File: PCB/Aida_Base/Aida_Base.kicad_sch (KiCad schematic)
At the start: 106 parts, among them J1 AudioJack4, J10 Conn_01x04_Pin, J2 USB_C_Receptacle_L, J3 Conn_01x02_Pin, J4 Conn_01x03_Pin, J5 Conn_01x04_Pin, J6 Conn_01x04_Pin, J7 Conn_01x02_Pin, J8 Conn_02x02_Odd_Even, J9 Conn_01x03_Pin, Q1 BSS138, SW1 BOOT, SW2 RESET, U1 NCP1117-3.3_SOT223, U2 RP2040_L, U3 W25Q128JVS, Y1 12MHz

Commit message: 左手の回路が完成
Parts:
- removed H6: MountingHole_Pad, symbol Mechanical:MountingHole_Pad
- added H_btm_L1, H_btm_L2, H_btm_L3, H_btm_L4, H_btm_L5, H_btm_L6: MountingHole, Lib_Local:MountingHole_2.2mm_M2_No_Cu, symbol Mechanical:MountingHole
- added H_mid_L1, H_mid_L2: MountingHole, Lib_Local:MountingHole_1.8-2.2mm_M2_Pad_minimal, symbol Mechanical:MountingHole_Pad
- R12: value 100 -> 330
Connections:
- net GND_L: now also H_mid_L1.1, H_mid_L2.1
- no-connect marks 11 -> 12
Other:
- note added: "SCREWS to Bottom Plate"
- note added: "SCREWS to Mid"
- note added: "TRRSに 保護回路が あってもよい"
- note added: "Topへの Col4は 下のスイッチ と共通"
- moved on the sheet: C16, C17, C18, C19, D22, J1, J10, J3, J4, J5, J6, J7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

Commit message: PCBの部品配置をやり始めた。左右の部品を仕分けした。
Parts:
- removed J3: Conn_01x02_Pin, symbol Connector:Conn_01x02_Pin
- removed J4: Conn_01x03_Pin, symbol Connector:Conn_01x03_Pin
- added C13, C14, C15, C16, C17, C18, C19, C20, C25, C26, C36, C37, C38: 100n, Capacitor_SMD:C_0402_1005Metric, symbol Device:C_Small
- added C24, C29, C30: 2.2uF, Capacitor_SMD:C_0402_1005Metric, symbol Device:C_Small
- added C3, C4: 10u, Capacitor_SMD:C_0805_2012Metric, symbol Device:C_Small
- added C35: 4.7u, Capacitor_SMD:C_0402_1005Metric, symbol Device:C_Small
- added D10, D11, D12, D18, D19, D20, D21, D22, D29, D30, D31, D32, D33, D34, D39, D40, D41, D42, D46, D7, D8, D9: D, Lib_Local:D_SOD-123_Emphasized_Direction_Line, symbol Device:D
- added D44: PRTR5V0U2X, Package_TO_SOT_SMD:SOT-143, symbol Power_Protection:PRTR5V0U2X
- added F2: Fuse, Fuse:Fuse_0603_1608Metric, symbol Device:Polyfuse_Small
- added H10, H11, H12, H14, H16, H18, H20, H4, H5, H6, H9: MountingHole_Pad, Lib_Local:MountingHole_1.8-2.2mm_M2_Pad_minimal, symbol Mechanical:MountingHole_Pad
- added H_btm_R1, H_btm_R2, H_btm_R3, H_btm_R4, H_btm_R5, H_btm_R6: MountingHole, Lib_Local:MountingHole_2.2mm_M2_No_Cu, symbol Mechanical:MountingHole
- added H_mid_R1, H_mid_R2: MountingHole, Lib_Local:MountingHole_1.8-2.2mm_M2_Pad_minimal, symbol Mechanical:MountingHole_Pad
- added J10: Conn_01x03_Pin, Connector_PinHeader_2.54mm:PinHeader_1x03_P2.54mm_Vertical, symbol Connector:Conn_01x03_Pin
- added J12, J14, J16: Conn_01x04_Pin, Connector_PinHeader_2.54mm:PinHeader_1x04_P2.54mm_Vertical, symbol Connector:Conn_01x04_Pin
- added J18: Conn_02x02_Odd_Even, Connector_PinHeader_2.54mm:PinHeader_2x02_P2.54mm_Vertical, symbol Connector_Generic:Conn_02x02_Odd_Even
- added J2: AudioJack4, Connector_Audio:Jack_3.5mm_PJ320E_Horizontal, symbol Connector_Audio:AudioJack4
- added J4: USB_C_Receptacle_R, Connector_USB:USB_C_Receptacle_HRO_TYPE-C-31-M-12, symbol Connector:USB_C_Receptacle
- added J6: Conn_01x02_Pin, Connector_PinHeader_2.54mm:PinHeader_1x02_P2.54mm_Vertical, symbol Connector:Conn_01x02_Pin
- added J7, J8: Conn_01x05_Pin, Connector_PinHeader_2.54mm:PinHeader_1x05_P2.54mm_Vertical, symbol Connector:Conn_01x05_Pin
- added JP2: SolderJumper_2_Open, Jumper:SolderJumper-2_P1.3mm_Open_RoundedPad1.0x1.5mm, symbol Jumper:SolderJumper_2_Open
- added L4, L5, L6: SK6812MINI-E, Lib_Local:YS-SK6812MINI-E_middle_hole_with_small_pad, symbol kbd:SK6812MINI-E
- added LS2: Speaker, Buzzer_Beeper:Buzzer_Murata_PKMCS0909E, symbol Device:Speaker
- added Q2: BSS138, Package_TO_SOT_SMD:SOT-23, symbol Transistor_FET:BSS138
- added R10, R13, R14, R17, R2, R22: 1k, Resistor_SMD:R_0402_1005Metric, symbol Device:R_Small
- added R18, R4: 330, Resistor_SMD:R_0402_1005Metric, symbol Device:R_Small
- added R20: 10k, Resistor_SMD:R_0402_1005Metric, symbol Device:R_Small
- added R24, R26: 4.7k, Resistor_SMD:R_0402_1005Metric, symbol Device:R_Small
- added R6, R8: 5.1k, Resistor_SMD:R_0402_1005Metric, symbol Device:R_Small
- added SD2: Schottky diode, Diode_SMD:D_SOD-123, symbol Device:D_Shockley
- added STLED2: LED_GREEN, LED_SMD:LED_0201_0603Metric_Pad0.64x0.40mm_HandSolder, symbol Device:LED_Small
- added SW2: BOOT, Button_Switch_SMD:SW_SPST_PTS810, symbol Switch:SW_Push
- added SW4: RESET, Button_Switch_SMD:SW_SPST_PTS810, symbol Switch:SW_Push
- added SW_A2, SW_B2, SW_C2, SW_CMD_L2, SW_CTL2, SW_D2, SW_E2, SW_F2, SW_OPT_L2, SW_S2, SW_SPC2, SW_V2, SW_W2, SW_X2, SW_Z2: SW_Push, Lib_Local:Kailh_socket_ChocV2, symbol Switch:SW_Push
- added SW_RE_L2: RotaryEncoder_Switch, Lib_Local:ChocV2_AND_RotaryEncoder_Alps_EC11K-Switch_Vertical_H20mm_NPTH_MP_minimal, symbol Device:RotaryEncoder_Switch
- added U2: NCP1117-3.3_SOT223, Package_TO_SOT_SMD:SOT-223-3_TabPin2, symbol Regulator_Linear:NCP1117-3.3_SOT223
- added U4: RP2040_R, Package_DFN_QFN:QFN-56-1EP_7x7mm_P0.4mm_EP3.2x3.2mm, symbol MCU_RaspberryPi:RP2040
- added U6: W25Q128JVS, Package_SO:SOIC-8_5.3x5.3mm_P1.27mm, symbol Memory_Flash:W25Q128JVS
- added Y2: 12MHz, Crystal:Resonator_SMD_Murata_CSTxExxV-3Pin_3.0x1.1mm, symbol Device:Crystal_GND2
- D1, D2, D3, D4, D5, D6: footprint Diode_SMD:D_SOD-128 -> Lib_Local:D_SOD-123_Emphasized_Direction_Line
- D13: renamed from D7; footprint Diode_SMD:D_SOD-128 -> Lib_Local:D_SOD-123_Emphasized_Direction_Line
- D14: renamed from D8; footprint Diode_SMD:D_SOD-128 -> Lib_Local:D_SOD-123_Emphasized_Direction_Line
- D15: renamed from D9; footprint Diode_SMD:D_SOD-128 -> Lib_Local:D_SOD-123_Emphasized_Direction_Line
- D16: renamed from D10; footprint Diode_SMD:D_SOD-128 -> Lib_Local:D_SOD-123_Emphasized_Direction_Line
- D17: renamed from D11; footprint Diode_SMD:D_SOD-128 -> Lib_Local:D_SOD-123_Emphasized_Direction_Line
- D23: renamed from D12; footprint Diode_SMD:D_SOD-128 -> Lib_Local:D_SOD-123_Emphasized_Direction_Line
- D24: renamed from D13; footprint Diode_SMD:D_SOD-128 -> Lib_Local:D_SOD-123_Emphasized_Direction_Line
- D25: renamed from D14; footprint Diode_SMD:D_SOD-128 -> Lib_Local:D_SOD-123_Emphasized_Direction_Line
- D26: renamed from D15; footprint Diode_SMD:D_SOD-128 -> Lib_Local:D_SOD-123_Emphasized_Direction_Line
- D27: renamed from D16; footprint Diode_SMD:D_SOD-128 -> Lib_Local:D_SOD-123_Emphasized_Direction_Line
- D28: renamed from D17; footprint Diode_SMD:D_SOD-128 -> Lib_Local:D_SOD-123_Emphasized_Direction_Line
- D35: renamed from D18; footprint Diode_SMD:D_SOD-128 -> Lib_Local:D_SOD-123_Emphasized_Direction_Line
- D36: renamed from D19; footprint Diode_SMD:D_SOD-128 -> Lib_Local:D_SOD-123_Emphasized_Direction_Line
- D37: renamed from D20; footprint Diode_SMD:D_SOD-128 -> Lib_Local:D_SOD-123_Emphasized_Direction_Line
- D38: renamed from D21; footprint Diode_SMD:D_SOD-128 -> Lib_Local:D_SOD-123_Emphasized_Direction_Line
- D45: renamed from D22; footprint (none) -> Lib_Local:D_SOD-123_Emphasized_Direction_Line
- H1, H2, H3: footprint (none) -> Lib_Local:MountingHole_1.8-2.2mm_M2_Pad_minimal
- H13: renamed from H7; footprint (none) -> Lib_Local:MountingHole_1.8-2.2mm_M2_Pad_minimal
- H15: renamed from H8; footprint (none) -> Lib_Local:MountingHole_1.8-2.2mm_M2_Pad_minimal
- H17: renamed from H9; footprint (none) -> Lib_Local:MountingHole_1.8-2.2mm_M2_Pad_minimal
- H19: renamed from H10; footprint (none) -> Lib_Local:MountingHole_1.8-2.2mm_M2_Pad_minimal
- H7: renamed from H4; footprint (none) -> Lib_Local:MountingHole_1.8-2.2mm_M2_Pad_minimal
- H8: renamed from H5; footprint (none) -> Lib_Local:MountingHole_1.8-2.2mm_M2_Pad_minimal
- J1: footprint (none) -> Connector_Audio:Jack_3.5mm_PJ320E_Horizontal
- J11: renamed from J5; footprint (none) -> Connector_PinHeader_2.54mm:PinHeader_1x04_P2.54mm_Vertical
- J13: renamed from J10; footprint (none) -> Connector_PinHeader_2.54mm:PinHeader_1x04_P2.54mm_Vertical
- J15: renamed from J6; footprint (none) -> Connector_PinHeader_2.54mm:PinHeader_1x04_P2.54mm_Vertical
- J17: renamed from J8; footprint (none) -> Connector_PinHeader_2.54mm:PinHeader_2x02_P2.54mm_Vertical
- J5: renamed from J7; footprint (none) -> Connector_PinHeader_2.54mm:PinHeader_1x02_P2.54mm_Vertical
- J9: footprint (none) -> Connector_PinHeader_2.54mm:PinHeader_1x03_P2.54mm_Vertical
- R1: footprint (none) -> Resistor_SMD:R_0402_1005Metric
- R16: renamed from R13; footprint (none) -> Resistor_SMD:R_0402_1005Metric
- R19: renamed from R8; footprint (none) -> Resistor_SMD:R_0402_1005Metric
- R21: renamed from R9; footprint (none) -> Resistor_SMD:R_0402_1005Metric
- R23: renamed from R10; footprint (none) -> Resistor_SMD:R_0402_1005Metric
- R25: renamed from R11; footprint (none) -> Resistor_SMD:R_0402_1005Metric
- R3: renamed from R12; footprint (none) -> Resistor_SMD:R_0402_1005Metric
- renumbered C8 to C10, C9 to C11, C10 to C12, C11 to C21, C14 to C22, C15 to C23, C12 to C27, C13 to C28, C16 to C31, C17 to C32, C18 to C33, C19 to C34, C3 to C5, C4 to C6, C5 to C7, C6 to C8, C7 to C9, D23 to D43, J2 to J3, R4 to R11, R5 to R12, R3 to R15, R6 to R5, R2 to R9, SW2 to SW3, U2 to U3, U3 to U5
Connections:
- net COL_L_4: now also H9.1
- net GPIO00 renamed GPIO00_L
- net GPIO00_L: now also J7.1 (Pin_1)
- net GPIO01 renamed GPIO01_L
- net GPIO01_L: now also J7.2 (Pin_2)
- net GPIO11 renamed GPIO11_L
- net GPIO11_L: now also J7.3 (Pin_3)
- net GPIO12 renamed GPIO12_L
- net GPIO12_L: now also J7.4 (Pin_4)
- net GPIO13 renamed GPIO13_L
- net GPIO13_L: now also J7.5 (Pin_5)
- net GPIO22 renamed GPIO22_L
- net GPIO23 renamed GPIO23_L
- net GPIO24 renamed GPIO24_L
- net GPIO25 renamed GPIO25_L
- net GPIO26 renamed GPIO26_L
- net GPIO27 renamed GPIO27_L
- net GPIO28 renamed GPIO28_L
- net GPIO29 renamed GPIO29_L
- new net: D8.2 (A), SW_W2.2
- new net: L4.4 (DIN), R18.2
- new net: LS2.1, R10.1
- new net: D20.2 (A), SW_D2.2
- new net: D40.2 (A), SW_CMD_L2.2
- new net: D19.2 (A), SW_S2.2
- new net: D7.2 (A), H4.1
- new net: J4.A5 (CC1), R6.1
- new net: D42.2 (A), SW_CTL2.2
- new net: R2.2, STLED2.2 (A)
- new net: D10.2 (A), H5.1
- new net: D32.2 (A), SW_V2.2
- new net: U4.20 (XIN), Y2.1
- new net: R17.1, Y2.3
- new net: JP2.2 (B), R2.1
- new net: D11.2 (A), H6.1
- new net: D29.2 (A), SW_Z2.2
- new net: D30.2 (A), SW_X2.2
- new net: J2.R1, R4.1
- new net: D18.2 (A), SW_A2.2
- new net: D39.2 (A), SW_OPT_L2.2
- new net: D21.2 (A), SW_F2.2
- new net: D34.2 (A), H18.1
- new net: D12.2 (A), SW_RE_L2.S2
- new net: L4.2 (DOUT), L5.4 (DIN)
- new net: L5.2 (DOUT), L6.4 (DIN)
- new net: J4.B5 (CC2), R8.1
- new net: F2.2, SD2.2 (A)
- new net: D9.2 (A), SW_E2.2
- new net: D31.2 (A), SW_C2.2
- new net: D33.2 (A), SW_B2.2
- new net: D22.2 (A), H14.1
- new net: R17.2, U4.21 (XOUT)
- new net: D41.2 (A), SW_SPC2.2
- new net +1V1_R: C25.1, C26.1, C30.1, U4.23 (DVDD), U4.45 (VREG_VOUT), U4.50 (DVDD)
- new net +3V3_R: C13.1, C14.1, C15.1, C16.1, C17.1, C18.1, C19.1, C20.1, C24.1, C29.1, C4.1, J14.1 (Pin_1), J6.2 (Pin_2), JP2.1 (A), Q2.1 (G), R13.2, R20.1, R24.1, R26.2, U2.2 (VO), U4.1 (IOVDD), U4.10 (IOVDD), U4.22 (IOVDD), U4.33 (IOVDD), U4.42 (IOVDD), U4.43 (ADC_AVDD), U4.44 (VREG_VIN), U4.48 (USB_VDD), U4.49 (IOVDD), U6.8 (VCC)
- new net +5V_R: C3.1, C35.2, C36.2, C37.2, C38.2, J2.T, J6.1 (Pin_1), L4.1 (VDD), L5.1 (VDD), L6.1 (VDD), R14.2, SD2.1 (K), U2.3 (VI)
- new net BUZZ_R: D46.1 (K), R10.2, U4.30 (GPIO19)
- new net COL_R_0: H10.1, SW_A2.1, SW_Z2.1, U4.8 (GPIO6)
- new net COL_R_1: SW_S2.1, SW_W2.1, SW_X2.1, U4.9 (GPIO7)
- new net COL_R_2: SW_C2.1, SW_D2.1, SW_E2.1, SW_OPT_L2.1, U4.11 (GPIO8)
- new net COL_R_3: H11.1, SW_CMD_L2.1, SW_F2.1, SW_V2.1, U4.12 (GPIO9)
- new net COL_R_4: H12.1, H16.1, SW_B2.1, SW_SPC2.1, U4.13 (GPIO10)
- new net COL_R_5: H20.1, SW_CTL2.1, SW_RE_L2.S1, U4.18 (GPIO15)
- new net D+_R: D44.2 (I/O1), J4.A6 (D+), J4.B6 (D+), U4.47 (USB_DP)
- new net D-_R: D44.3 (I/O2), J4.A7 (D-), J4.B7 (D-), U4.46 (USB_DM)
- new net DATA_R: R4.2, U4.17 (GPIO14)
- new net ENC_R_A: SW_RE_L2.A, U4.28 (GPIO17)
- new net ENC_R_B: SW_RE_L2.B, U4.29 (GPIO18)
- new net GND_R: C13.2, C14.2, C15.2, C16.2, C17.2, C18.2, C19.2, C20.2, C24.2, C25.2, C26.2, C29.2, C3.2, C30.2, C35.1, C36.1, C37.1, C38.1, C4.2, D44.1 (GND), D46.2 (A), H_mid_R1.1, H_mid_R2.1, J10.2 (Pin_2), J14.4 (Pin_4), J18.2 (Pin_2), J18.4 (Pin_4), J2.R2, J2.S, J4.A1 (GND), J4.A12 (GND), J4.B1 (GND), J4.B12 (GND), J4.S1 (SHIELD), L4.3 (GND), L5.3 (GND), L6.3 (GND), LS2.2, R6.2, R8.2, STLED2.1 (K), SW2.2, SW4.2, SW_RE_L2.C, U2.1 (GND), U4.19 (TESTEN), U4.57 (GND), U6.4 (GND), Y2.2
- new net GPIO00_R: J8.1 (Pin_1), U4.2 (GPIO0)
- new net GPIO01_R: J8.2 (Pin_2), U4.3 (GPIO1)
- new net GPIO11_R: J8.3 (Pin_3), U4.14 (GPIO11)
- new net GPIO12_R: J8.4 (Pin_4), U4.15 (GPIO12)
- new net GPIO13_R: J8.5 (Pin_5), U4.16 (GPIO13)
- new net GPIO22_R: J12.1 (Pin_1), U4.34 (GPIO22)
- new net GPIO23_R: J12.2 (Pin_2), U4.35 (GPIO23)
- new net GPIO24_R: J12.3 (Pin_3), U4.36 (GPIO24)
- new net GPIO25_R: J12.4 (Pin_4), U4.37 (GPIO25)
- new net GPIO26_R: J16.1 (Pin_1), U4.38 (GPIO26/ADC0)
- new net GPIO27_R: J16.2 (Pin_2), U4.39 (GPIO27/ADC1)
- new net GPIO28_R: J16.3 (Pin_3), U4.40 (GPIO28/ADC2)
- new net GPIO29_R: J16.4 (Pin_4), U4.41 (GPIO29/ADC3)
- new net LED_3V3_R: Q2.2 (S), R13.1, U4.27 (GPIO16)
- new net LED_5V_R: Q2.3 (D), R14.1, R18.1
- new net QSPI_SCLK_R: U4.52 (QSPI_SCLK), U6.6 (CLK)
- new net QSPI_SD0_R: U4.53 (QSPI_SD0), U6.5 (DI/IO_{0})
- new net QSPI_SD1_R: U4.55 (QSPI_SD1), U6.2 (DO/IO_{1})
- new net QSPI_SD2_R: U4.54 (QSPI_SD2), U6.3 (~{WP}/IO_{2})
- new net QSPI_SD3_R: U4.51 (QSPI_SD3), U6.7 (~{HOLD}/~{RESET}/IO_{3})
- new net QSPI_SS_R: R20.2, R22.1, U4.56 (~{QSPI_SS}), U6.1 (~{CS})
- new net RESET_R: J18.3 (Pin_3), SW4.1, U4.26 (RUN)
- new net ROW_R_0: D10.1 (K), D11.1 (K), D12.1 (K), D7.1 (K), D8.1 (K), D9.1 (K), U4.4 (GPIO2)
- new net ROW_R_1: D18.1 (K), D19.1 (K), D20.1 (K), D21.1 (K), D22.1 (K), U4.5 (GPIO3)
- new net ROW_R_2: D29.1 (K), D30.1 (K), D31.1 (K), D32.1 (K), D33.1 (K), D34.1 (K), U4.6 (GPIO4)
- new net ROW_R_3: D39.1 (K), D40.1 (K), D41.1 (K), D42.1 (K), U4.7 (GPIO5)
- new net SCL_R: J14.3 (Pin_3), R26.1, U4.32 (GPIO21)
- new net SDA_R: J14.2 (Pin_2), R24.2, U4.31 (GPIO20)
- new net SWCLK_R: J10.1 (Pin_1), U4.24 (SWCLK)
- new net SWDIO_R: J10.3 (Pin_3), U4.25 (SWDIO)
- new net USB_BOOT_R: J18.1 (Pin_1), R22.2, SW2.1
- new net VBUS_R: D44.4 (VCC), F2.1, J4.A4 (VBUS), J4.A9 (VBUS), J4.B4 (VBUS), J4.B9 (VBUS)
- no-connect marks 12 -> 22
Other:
- moved on the sheet: J11, J15

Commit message: 左手パーツ配置中。右手マトリクス修正
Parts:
- removed SW_A2, SW_B2, SW_C2, SW_CMD_L2, SW_CTL2, SW_D2, SW_E2, SW_F2, SW_OPT_L2, SW_S2, SW_SPC2, SW_V2, SW_W2, SW_X2, SW_Z2: SW_Push, Lib_Local:Kailh_socket_ChocV2, symbol Switch:SW_Push
- added SW_-1, SW_/1, SW_<1, SW_>1, SW_BS1, SW_CMD_R1, SW_ENT1, SW_I1, SW_J1, SW_K1, SW_L1, SW_M1, SW_N1, SW_O1, SW_OPT_R1: SW_Push, Lib_Local:Kailh_socket_ChocV2, symbol Switch:SW_Push
- D6, H10, SW_RE_L1: now not fitted
- H1: value MountingHole_Pad -> COL_L_0_from_Mid_Outside
- H12: now fitted
- H13: value MountingHole_Pad -> COL_L_4_from_Mid_Inside
- H15: value MountingHole_Pad -> COL_L_4_to_Mid_Inside
- H17: value MountingHole_Pad -> COL_L_5_from_Mid_Inside
- H19: value MountingHole_Pad -> COL_L_5_to_Mid_Inside
- H2: value MountingHole_Pad -> COL_L_3_from_Mid_Inside
- H3: value MountingHole_Pad -> COL_L_4_from_Top
- H7: value MountingHole_Pad -> COL_L_0_to_Mid_Outside
- H8: value MountingHole_Pad -> COL_L_3_to_Mid_Inside
- J11, J12, J15, J16: footprint Connector_PinHeader_2.54mm:PinHeader_1x04_P2.54mm_Vertical -> Connector_PinHeader_1.00mm:PinHeader_1x04_P1.00mm_Vertical
- J17, J18: footprint Connector_PinHeader_2.54mm:PinHeader_2x02_P2.54mm_Vertical -> Connector_PinHeader_2.00mm:PinHeader_2x02_P2.00mm_Vertical
- J5, J6: footprint Connector_PinHeader_2.54mm:PinHeader_1x02_P2.54mm_Vertical -> Connector_PinHeader_2.00mm:PinHeader_1x02_P2.00mm_Vertical
- J7, J8: footprint Connector_PinHeader_2.54mm:PinHeader_1x05_P2.54mm_Vertical -> Connector_PinHeader_1.00mm:PinHeader_1x05_P1.00mm_Vertical
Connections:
- net COL_R_0: now also H12.1, SW_-1.1, SW_/1.1; no longer H10.1
- net COL_R_1: now also SW_>1.1, SW_L1.1, SW_O1.1
- net COL_R_2: now also SW_<1.1, SW_I1.1, SW_K1.1, SW_OPT_R1.1
- net COL_R_3: now also SW_CMD_R1.1, SW_J1.1, SW_M1.1
- net COL_R_4: now also H10.1, SW_ENT1.1, SW_N1.1; no longer H12.1
- net COL_R_5: now also SW_BS1.1
- net at D8.2 (A): now also H4.1
- net at D20.2 (A): now also SW_K1.2
- net at D40.2 (A): now also SW_ENT1.2
- net at D19.2 (A): now also SW_J1.2
- net at D7.2 (A): now also SW_RE_L2.S2; no longer H4.1
- net at D42.2 (A): now also SW_OPT_R1.2
- net at D10.2 (A): now also SW_I1.2; no longer H5.1
- net at D32.2 (A): now also SW_<1.2
- net at D11.2 (A): now also SW_O1.2; no longer H6.1
- net at D29.2 (A): now also H18.1
- net at D30.2 (A): now also SW_N1.2
- net at D18.2 (A): now also H14.1
- net at D39.2 (A): now also SW_BS1.2
- net at D21.2 (A): now also SW_L1.2
- net at D34.2 (A): now also SW_/1.2; no longer H18.1
- net at D12.2 (A): now also H6.1; no longer SW_RE_L2.S2
- net at D9.2 (A): now also H5.1
- net at D31.2 (A): now also SW_M1.2
- net at D33.2 (A): now also SW_>1.2
- net at D22.2 (A): now also SW_-1.2; no longer H14.1
- net at D41.2 (A): now also SW_CMD_R1.2
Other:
- moved on the sheet: C1, C2, C3, C4

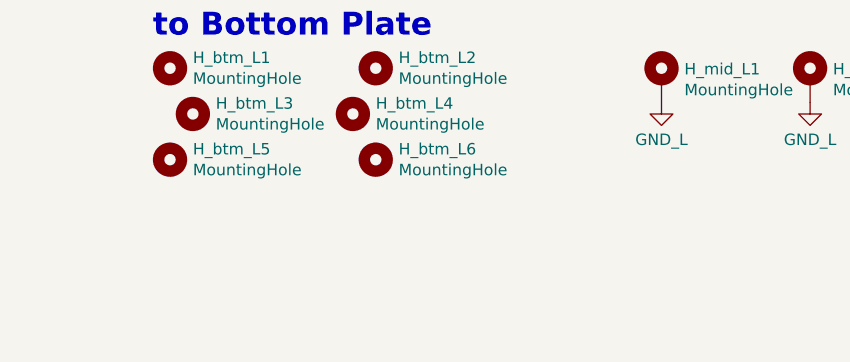
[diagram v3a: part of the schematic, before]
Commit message: 左手パーツ配置中。ネジ位置で悩み中。
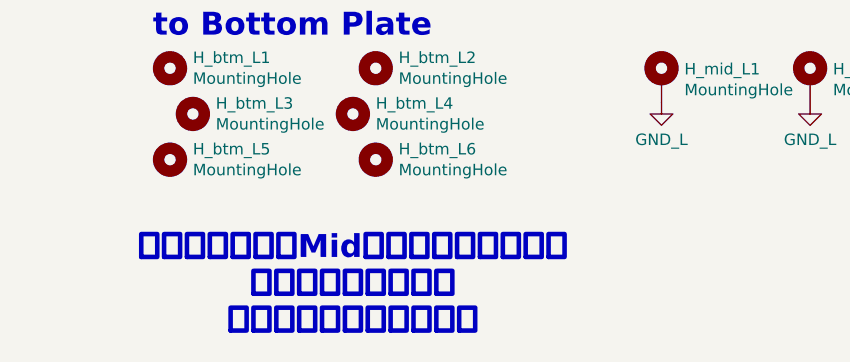
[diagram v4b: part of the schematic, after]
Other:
- note added: "マトリクス内のMidねじ＝ボトム用ねじ の場合があるので、 こちらは少し減らす予定"
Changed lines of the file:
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@@
+		)
+	)
+	(text "マトリクス内のMidねじ＝ボトム用ねじ\nの場合があるので、\nこちらは少し減らす予定"
+		(exclude_from_sim no)
+		(at 36.83 289.56 0)
+		(effects
+			(font
+				(size 2.54 2.54)
+				(thickness 0.508)
+				(bold yes)
+				(color 255 0 0 1)
+			)
 		)
 	)

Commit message: 左手パーツ配置中。ネジ位置ほぼ確定。MCUまわり配置中。
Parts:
- H1, H11, H12, H13, H14, H15, H16, H17, H18, H19, H2, H20, H3, H4, H5, H6, H7, H8, H_mid_L1, H_mid_L2, H_mid_R1, H_mid_R2: footprint Lib_Local:MountingHole_1.8-2.2mm_M2_Pad_minimal -> Lib_Local:MountingHole_M2_Through-hole_tap_THC-0.8-2.0-2_minimal
- H_btm_L1, H_btm_L2, H_btm_L3, H_btm_L4, H_btm_L5, H_btm_L6, H_btm_R1, H_btm_R2, H_btm_R3, H_btm_R4, H_btm_R5, H_btm_R6: footprint Lib_Local:MountingHole_2.2mm_M2_No_Cu -> Lib_Local:MountingHole_M2_Through-hole_tap_THC-0.8-1.0-2_minimal
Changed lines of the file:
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@@
 			)
 		)
-		(property "Footprint" "Lib_Local:MountingHole_2.2mm_M2_No_Cu"
+		(property "Footprint" "Lib_Local:MountingHole_M2_Through-hole_tap_THC-0.8-1.0-2_minimal"
 			(at 16.51 265.43 0)
 			(effects
@@
 			)
 		)
-		(property "Footprint" "Lib_Local:MountingHole_1.8-2.2mm_M2_Pad_minimal"
+		(property "Footprint" "Lib_Local:MountingHole_M2_Through-hole_tap_THC-0.8-2.0-2_minimal"
 			(at 186.69 62.23 0)
 			(effects
@@
 			)
 		)
-		(property "Footprint" "Lib_Local:MountingHole_1.8-2.2mm_M2_Pad_minimal"
+		(property "Footprint" "Lib_Local:MountingHole_M2_Through-hole_tap_THC-0.8-2.0-2_minimal"
 			(at 161.29 36.83 0)
 			(effects
@@
 			)
 		)
-		(property "Footprint" "Lib_Local:MountingHole_1.8-2.2mm_M2_Pad_minimal"
+		(property "Footprint" "Lib_Local:MountingHole_M2_Through-hole_tap_THC-0.8-2.0-2_minimal"
 			(at 168.91 53.34 0)
 			(effects
@@
 			)
 		)
-		(property "Footprint" "Lib_Local:MountingHole_1.8-2.2mm_M2_Pad_minimal"
+		(property "Footprint" "Lib_Local:MountingHole_M2_Through-hole_tap_THC-0.8-2.0-2_minimal"
 			(at 340.36 36.83 0)
 			(effects
@@
 			)
 		)
-		(property "Footprint" "Lib_Local:MountingHole_1.8-2.2mm_M2_Pad_minimal"
+		(property "Footprint" "Lib_Local:MountingHole_M2_Through-hole_tap_THC-0.8-2.0-2_minimal"
 			(at 118.11 40.64 0)
 			(effects
@@
 			)
 		)
-		(property "Footprint" "Lib_Local:MountingHole_1.8-2.2mm_M2_Pad_minimal"
+		(property "Footprint" "Lib_Local:MountingHole_M2_Through-hole_tap_THC-0.8-2.0-2_minimal"
 			(at 335.28 53.34 0)
 			(effects
@@
 			)
 		)
-		(property "Footprint" "Lib_Local:MountingHole_1.8-2.2mm_M2_Pad_minimal"
+		(property "Footprint" "Lib_Local:MountingHole_M2_Through-hole_tap_THC-0.8-2.0-2_minimal"
 			(at 322.58 66.04 0)
 			(effects
@@
 			)
 		)
-		(property "Footprint" "Lib_Local:MountingHole_2.2mm_M2_No_Cu"
+		(property "Footprint" "Lib_Local:MountingHole_M2_Through-hole_tap_THC-0.8-1.0-2_minimal"
 			(at 214.63 275.59 0)
 			(effects
@@
 			)
 		)
-		(property "Footprint" "Lib_Local:MountingHole_1.8-2.2mm_M2_Pad_minimal"
+		(property "Footprint" "Lib_Local:MountingHole_M2_Through-hole_tap_THC-0.8-2.0-2_minimal"
 			(at 386.08 40.64 0)
 			(effects
@@
 			)
 		)
-		(property "Footprint" "Lib_Local:MountingHole_1.8-2.2mm_M2_Pad_minimal"
+		(property "Footprint" "Lib_Local:MountingHole_M2_Through-hole_tap_THC-0.8-2.0-2_minimal"
 			(at 71.12 266.7 0)
 			(effects
@@
 			)
 		)
-		(property "Footprint" "Lib_Local:MountingHole_2.2mm_M2_No_Cu"
+		(property "Footprint" "Lib_Local:MountingHole_M2_Through-hole_tap_THC-0.8-1.0-2_minimal"
 			(at 39.37 275.59 0)
 			(effects
@@
 			)
 		)
-		(property "Footprint" "Lib_Local:MountingHole_1.8-2.2mm_M2_Pad_minimal"
+		(property "Footprint" "Lib_Local:MountingHole_M2_Through-hole_tap_THC-0.8-2.0-2_minimal"
 			(at 340.36 49.53 0)
 			(effects
@@
 			)
 		)
-		(property "Footprint" "Lib_Local:MountingHole_1.8-2.2mm_M2_Pad_minimal"
+		(property "Footprint" "Lib_Local:MountingHole_M2_Through-hole_tap_THC-0.8-2.0-2_minimal"
 			(at 173.99 36.83 0)
 			(effects
@@
 			)
 		)
-		(property "Footprint" "Lib_Local:MountingHole_1.8-2.2mm_M2_Pad_minimal"
+		(property "Footprint" "Lib_Local:MountingHole_M2_Through-hole_tap_THC-0.8-2.0-2_minimal"
 			(at 391.16 36.83 0)
 			(effects
@@
 			)
 		)
-		(property "Footprint" "Lib_Local:MountingHole_1.8-2.2mm_M2_Pad_minimal"
+		(property "Footprint" "Lib_Local:MountingHole_M2_Through-hole_tap_THC-0.8-2.0-2_minimal"
 			(at 156.21 40.64 0)
 			(effects
@@
 			)
 		)
-		(property "Footprint" "Lib_Local:MountingHole_2.2mm_M2_No_Cu"
+		(property "Footprint" "Lib_Local:MountingHole_M2_Through-hole_tap_THC-0.8-1.0-2_minimal"
 			(at 19.05 270.51 0)
 			(effects
@@
 			)
 		)
-		(property "Footprint" "Lib_Local:MountingHole_1.8-2.2mm_M2_Pad_minimal"
+		(property "Footprint" "Lib_Local:MountingHole_M2_Through-hole_tap_THC-0.8-2.0-2_minimal"
 			(at 327.66 62.23 0)
 			(effects
@@
 			)
 		)
-		(property "Footprint" "Lib_Local:MountingHole_1.8-2.2mm_M2_Pad_minimal"
+		(property "Footprint" "Lib_Local:MountingHole_M2_Through-hole_tap_THC-0.8-2.0-2_minimal"
 			(at 269.24 266.7 0)
 			(effects
@@
 			)
 		)
-		(property "Footprint" "Lib_Local:MountingHole_2.2mm_M2_No_Cu"
+		(property "Footprint" "Lib_Local:MountingHole_M2_Through-hole_tap_THC-0.8-1.0-2_minimal"
 			(at 16.51 275.59 0)
 			(effects
@@
 			)
 		)
-		(property "Footprint" "Lib_Local:MountingHole_2.2mm_M2_No_Cu"
+		(property "Footprint" "Lib_Local:MountingHole_M2_Through-hole_tap_THC-0.8-1.0-2_minimal"
 			(at 39.37 265.43 0)
 			(effects
@@
 			)
 		)
-		(property "Footprint" "Lib_Local:MountingHole_1.8-2.2mm_M2_Pad_minimal"
+		(property "Footprint" "Lib_Local:MountingHole_M2_Through-hole_tap_THC-0.8-2.0-2_minimal"
 			(at 347.98 40.64 0)
 			(effects
@@
 			)
 		)
-		(property "Footprint" "Lib_Local:MountingHole_1.8-2.2mm_M2_Pad_minimal"
+		(property "Footprint" "Lib_Local:MountingHole_M2_Through-hole_tap_THC-0.8-2.0-2_minimal"
 			(at 123.19 36.83 0)
 			(effects
@@
 			)
 		)
-		(property "Footprint" "Lib_Local:MountingHole_2.2mm_M2_No_Cu"
+		(property "Footprint" "Lib_Local:MountingHole_M2_Through-hole_tap_THC-0.8-1.0-2_minimal"
 			(at 214.63 265.43 0)
 			(effects
@@
 			)
 		)
-		(property "Footprint" "Lib_Local:MountingHole_1.8-2.2mm_M2_Pad_minimal"
+		(property "Footprint" "Lib_Local:MountingHole_M2_Through-hole_tap_THC-0.8-2.0-2_minimal"
 			(at 181.61 66.04 0)
 			(effects
@@
 			)
 		)
-		(property "Footprint" "Lib_Local:MountingHole_2.2mm_M2_No_Cu"
+		(property "Footprint" "Lib_Local:MountingHole_M2_Through-hole_tap_THC-0.8-1.0-2_minimal"
 			(at 234.95 270.51 0)
 			(effects
@@
 			)
 		)
-		(property "Footprint" "Lib_Local:MountingHole_2.2mm_M2_No_Cu"
+		(property "Footprint" "Lib_Local:MountingHole_M2_Through-hole_tap_THC-0.8-1.0-2_minimal"
 			(at 237.49 275.59 0)
 			(effects
@@
 			)
 		)
-		(property "Footprint" "Lib_Local:MountingHole_1.8-2.2mm_M2_Pad_minimal"
+		(property "Footprint" "Lib_Local:MountingHole_M2_Through-hole_tap_THC-0.8-2.0-2_minimal"
 			(at 87.63 266.7 0)
 			(effects
@@
 			)
 		)
-		(property "Footprint" "Lib_Local:MountingHole_1.8-2.2mm_M2_Pad_minimal"
+		(property "Footprint" "Lib_Local:MountingHole_M2_Through-hole_tap_THC-0.8-2.0-2_minimal"
 			(at 353.06 36.83 0)
 			(effects
@@
 			)
 		)
-		(property "Footprint" "Lib_Local:MountingHole_2.2mm_M2_No_Cu"
+		(property "Footprint" "Lib_Local:MountingHole_M2_Through-hole_tap_THC-0.8-1.0-2_minimal"
 			(at 36.83 270.51 0)
 			(effects
@@
 			)
 		)
-		(property "Footprint" "Lib_Local:MountingHole_1.8-2.2mm_M2_Pad_minimal"
+		(property "Footprint" "Lib_Local:MountingHole_M2_Through-hole_tap_THC-0.8-2.0-2_minimal"
 			(at 285.75 266.7 0)
 			(effects
@@
 			)
 		)
-		(property "Footprint" "Lib_Local:MountingHole_1.8-2.2mm_M2_Pad_minimal"
+		(property "Footprint" "Lib_Local:MountingHole_M2_Through-hole_tap_THC-0.8-2.0-2_minimal"
 			(at 173.99 49.53 0)
 			(effects
@@
 			)
 		)
-		(property "Footprint" "Lib_Local:MountingHole_2.2mm_M2_No_Cu"
+		(property "Footprint" "Lib_Local:MountingHole_M2_Through-hole_tap_THC-0.8-1.0-2_minimal"
 			(at 237.49 265.43 0)
 			(effects
@@
 			)
 		)
-		(property "Footprint" "Lib_Local:MountingHole_2.2mm_M2_No_Cu"
+		(property "Footprint" "Lib_Local:MountingHole_M2_Through-hole_tap_THC-0.8-1.0-2_minimal"
 			(at 217.17 270.51 0)
 			(effects

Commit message: 基板4枚、位置決め完了。
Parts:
- removed C21, C24: 2.2uF, Capacitor_SMD:C_0402_1005Metric, symbol Device:C_Small
- removed H_btm_L1, H_btm_L2, H_btm_R1, H_btm_R2: MountingHole, Lib_Local:MountingHole_M2_Through-hole_tap_THC-0.8-1.0-2_minimal, symbol Mechanical:MountingHole
- removed U1, U2: NCP1117-3.3_SOT223, Package_TO_SOT_SMD:SOT-223-3_TabPin2, symbol Regulator_Linear:NCP1117-3.3_SOT223
- added R27, R28, R29, R30: 27, Resistor_SMD:R_0402_1005Metric, symbol Device:R_Small
- added U7, U8: AP2112K-3.3, Package_TO_SOT_SMD:SOT-23-5, symbol Regulator_Linear:AP2112K-3.3
- C27, C28, C29, C30: value 2.2uF -> 1u
- J1, J2: footprint Connector_Audio:Jack_3.5mm_PJ320E_Horizontal -> Lib_Local:TRRS-PJ-320A
- U3, U4: footprint Package_DFN_QFN:QFN-56-1EP_7x7mm_P0.4mm_EP3.2x3.2mm -> Lib_Local:RP2040-QFN-56
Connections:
- net +3V3_L: now also U7.5 (VOUT)
- net +3V3_R: now also U8.5 (VOUT)
- net +5V_L: now also U7.1 (VIN), U7.3 (EN)
- net +5V_R: now also U8.1 (VIN), U8.3 (EN)
- net D+_L: now also R29.1; no longer U3.47 (USB_DP)
- net D+_R: now also R30.1; no longer U4.47 (USB_DP)
- net D-_L: now also R27.1; no longer U3.46 (USB_DM)
- net D-_R: now also R28.1; no longer U4.46 (USB_DM)
- net GND_L: now also U7.2 (GND)
- net GND_R: now also U8.2 (GND)
- new net: R27.2, U3.46 (USB_DM)
- new net: R28.2, U4.46 (USB_DM)
- new net: R30.2, U4.47 (USB_DP)
- new net: R29.2, U3.47 (USB_DP)

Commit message: 右手パーツ配置中
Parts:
- C1, C2, C3, C4: footprint Capacitor_SMD:C_0805_2012Metric -> Capacitor_SMD:C_0402_1005Metric; LCSC C15850 -> C15525
- H11: value MountingHole_Pad -> COL_R_3_to_Mid
- H12: value MountingHole_Pad -> COL_R_0_to_Mid_Outside
- H14: value MountingHole_Pad -> COL_R_4_from_Mid
- H16: value MountingHole_Pad -> COL_R_4_to_Mid/Top
- H18: value MountingHole_Pad -> COL_R_5_from_Mid
- H20: value MountingHole_Pad -> COL_R_5_to_Mid
- H4: value MountingHole_Pad -> COL_R_4_from_Top
- H5: value MountingHole_Pad -> COL_R_3_from_Mid
- H6: value MountingHole_Pad -> COL_R_0_from_Mid_Outside
- H_btm_L3, H_btm_L4, H_btm_L5, H_btm_L6, H_btm_R3, H_btm_R4, H_btm_R5, H_btm_R6: symbol Mechanical:MountingHole -> Mechanical:MountingHole_Pad; now left out of the parts list
- H_mid_L1, H_mid_L2, H_mid_R1, H_mid_R2: footprint Lib_Local:MountingHole_M2_Through-hole_tap_THC-0.8-2.0-2_minimal -> Lib_Local:MountingHole_M2_Through-hole_tap_THC-0.8-1.0-2_minimal
- J1, J2: footprint Lib_Local:TRRS-PJ-320A -> Lib_Local:TRRS-PJ-320A_PinNameChanged
- J3, J4: symbol Connector:USB_C_Receptacle -> Connector:USB_C_Receptacle_USB2.0_14P
- J5, J6: footprint Connector_PinHeader_2.00mm:PinHeader_1x02_P2.00mm_Vertical -> Connector_PinHeader_2.00mm:PinHeader_1x03_P2.00mm_Vertical; symbol Connector:Conn_01x02_Pin -> Connector:Conn_01x03_Pin
- SW_RE_L2: now not fitted
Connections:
- net +3V3_L: now also J5.3 (Pin_3); no longer J5.2 (Pin_2)
- net +3V3_R: now also J6.3 (Pin_3); no longer J6.2 (Pin_2)
- net GND_L: now also H_btm_L3.1, H_btm_L4.1, H_btm_L5.1, H_btm_L6.1, J5.2 (Pin_2)
- net GND_R: now also H_btm_R3.1, H_btm_R4.1, H_btm_R5.1, H_btm_R6.1, J6.2 (Pin_2)
- no-connect marks 22 -> 2
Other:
- moved on the sheet: R5, R6, R7, R8
